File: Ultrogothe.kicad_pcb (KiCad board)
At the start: 2 copper layers, 20.3 x 54.6 mm, 18 parts, among them J1 Conn_01x20, J2 Conn_01x20, J3 Conn_02x05_Odd_Even, U1 XC6206PxxxMR, U2 STM32F103CBTx, Y1 Crystal

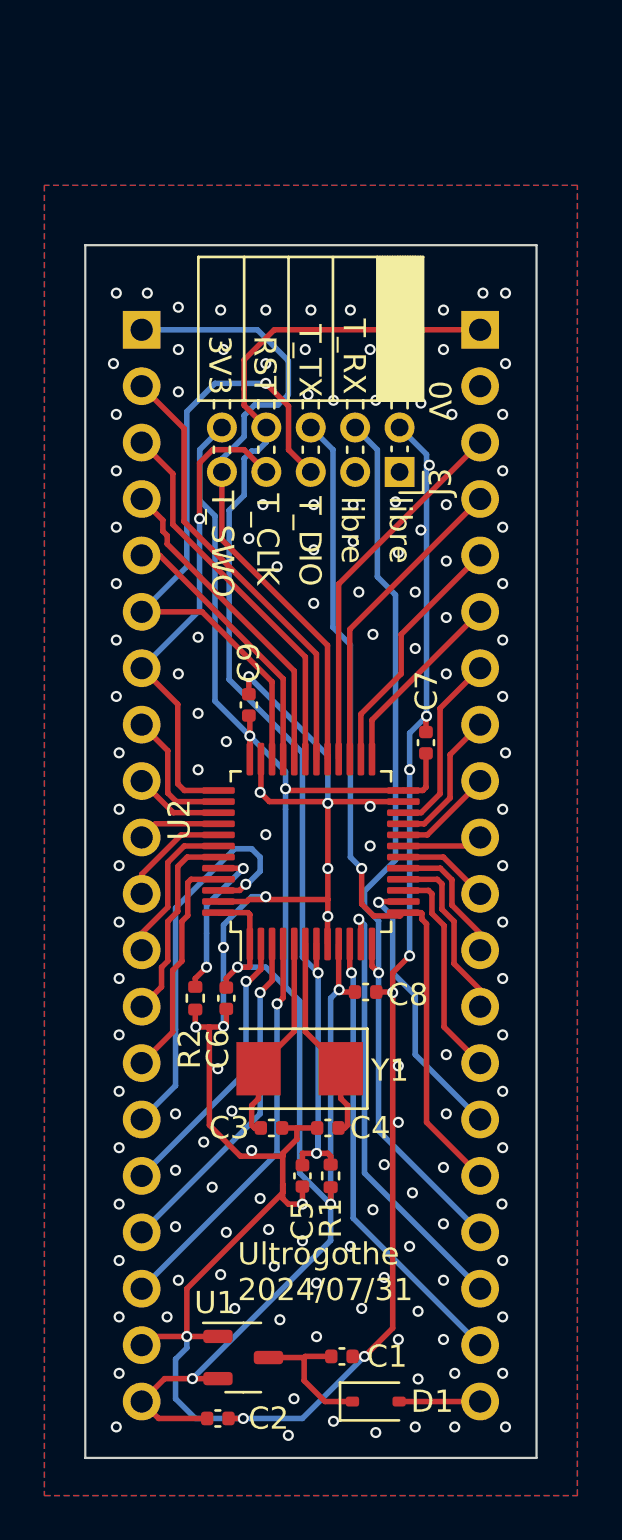
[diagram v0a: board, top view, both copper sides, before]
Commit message: Passage à kicad 8
et correction des chemins spécifiques
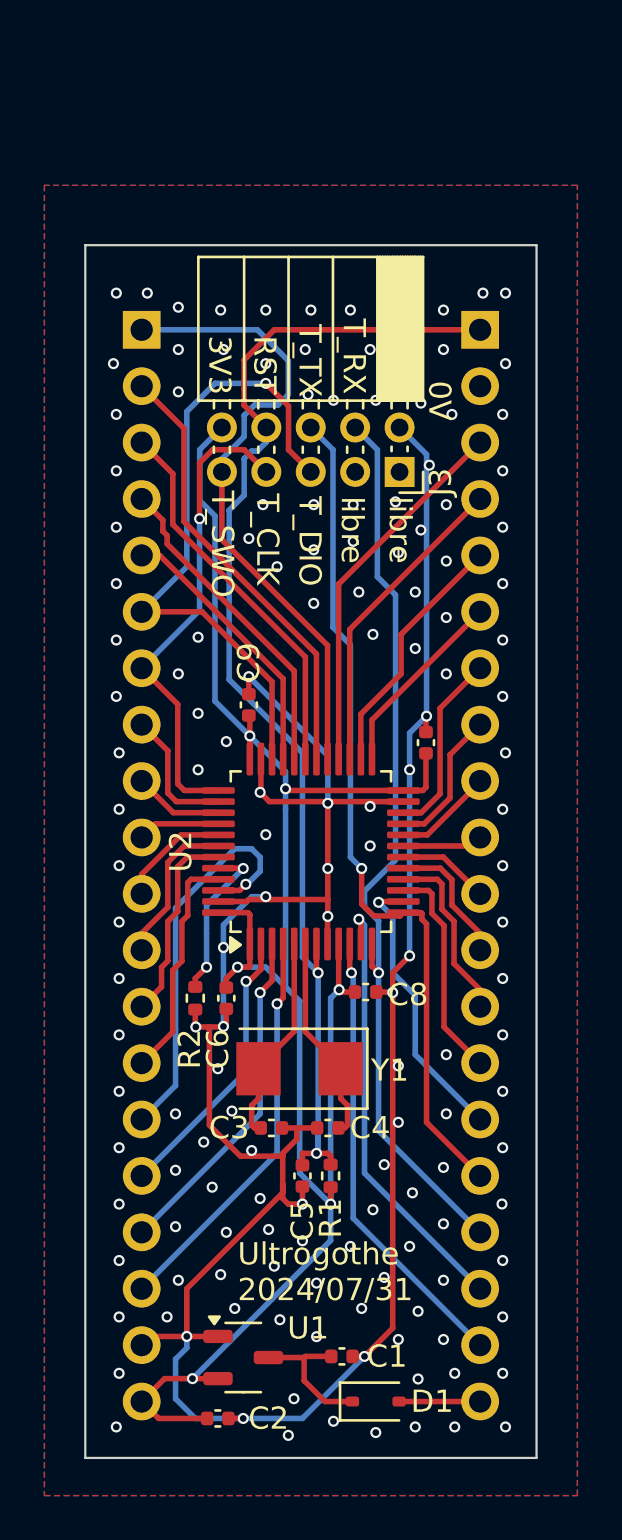
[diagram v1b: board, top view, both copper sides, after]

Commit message: Chgt connecteur programmation
passage à 2,54mm
alignement avec grille
silk: ajout pins
maj schéma pour clarification
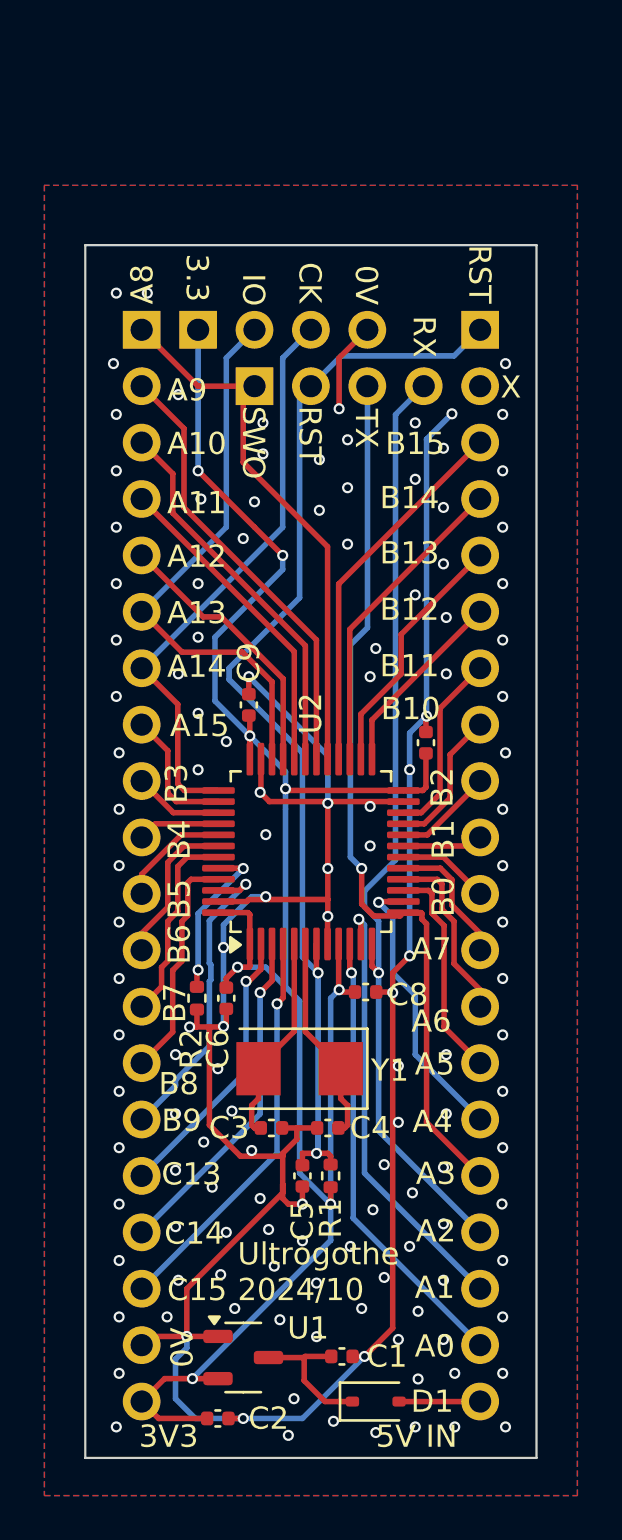
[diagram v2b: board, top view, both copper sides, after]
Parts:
- added J4: Conn_01x04, Chimere_comps:PinHeader_1x04_P2.54mm_Simple, B.Cu at (132.1, 53.3)
- J1, J2: footprint Connector_PinHeader_2.54mm:PinHeader_1x20_P2.54mm_Vertical -> Chimere_comps:PinHeader_1x20_P2.54mm_Simple
- J3: value Conn_02x05_Odd_Even -> Conn_01x04; footprint Connector_PinSocket_2.00mm:PinSocket_2x05_P2.00mm_Horizontal -> Chimere_comps:PinHeader_1x04_P2.54mm_Simple; moved to B.Cu
- moved J3 11.1 mm to (129.5, 50.8)
- moved R2 0.08 mm to (129.5, 80.9)
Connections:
- net /s_debugger/5V renamed /s_Alimentation/5V
- J3 pad 1: unconnected-(J3-Pin_1-Pad1) -> 3V3
- J3 pad 2: 0V -> A13
- J3 pad 3: unconnected-(J3-Pin_3-Pad3) -> A14
- J3 pad 4: A2 -> 0V
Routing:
- net 3V3: track 86.7 -> 93.2 mm, vias 6 -> 8
- net 0V: track 124.0 -> 128.9 mm, vias 153 -> 137
- net A14: track 21.8 -> 26.2 mm, vias 1 -> 0
- net B9: track 18.1 -> 13.9 mm
- net A13: track 29.4 -> 25.5 mm, vias 1 -> 0
- net A8: track 28.9 -> 25.4 mm
- net nRST: track 53.9 -> 50.4 mm
- net A2: track 41.2 -> 42.8 mm
- net A3: track 38.3 -> 39.8 mm
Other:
- board text added: "3.3"
- board text added: "5V IN"
- board text added: "A0"
- board text added: "A1"
- board text added: "A10"
- board text added: "A11"
- board text added: "A12"
- board text added: "A13"
- board text added: "A14"
- board text added: "A15"
- board text added: "A2"
- board text added: "A3"
- board text added: "A4"
- board text added: "A5"
- board text added: "A6"
- board text added: "A7"
- board text added: "A8"
- board text added: "A9"
- board text added: "B0"
- board text added: "B1"
- board text added: "B10"
- board text added: "B11"
- board text added: "B12"
- board text added: "B13"
- board text added: "B14"
- board text added: "B15"
- board text added: "B2"
- board text added: "B3"
- board text added: "B4"
- board text added: "B5"
- board text added: "B6"
- board text added: "B7"
- board text added: "B8"
- board text added: "B9"
- board text added: "C13"
- board text added: "C14"
- board text added: "C15"
- board text added: "CK"
- board text added: "IO"
- board text added: "RX"
- board text added: "SWO"
- board text added: "TX"
- board text added: "Ultrogothe 2024/10"
- board text added: "Ultrogothe 2024/10/23"
- board text added: "X"
- board text removed: "T_CLK"
- board text removed: "T_DIO"
- board text removed: "T_RX"
- board text removed: "T_SWO"
- board text removed: "T_TX"
- board text removed: "Ultrogothe 2024/07/31"
- board text removed: "libre"

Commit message: vias et plans cuivres
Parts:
- moved C2 0.13 mm to (130.4, 99.7)
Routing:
- net 3V3: track 93.2 -> 84.4 mm
- net 0V: track 128.9 -> 131.5 mm, vias 137 -> 196

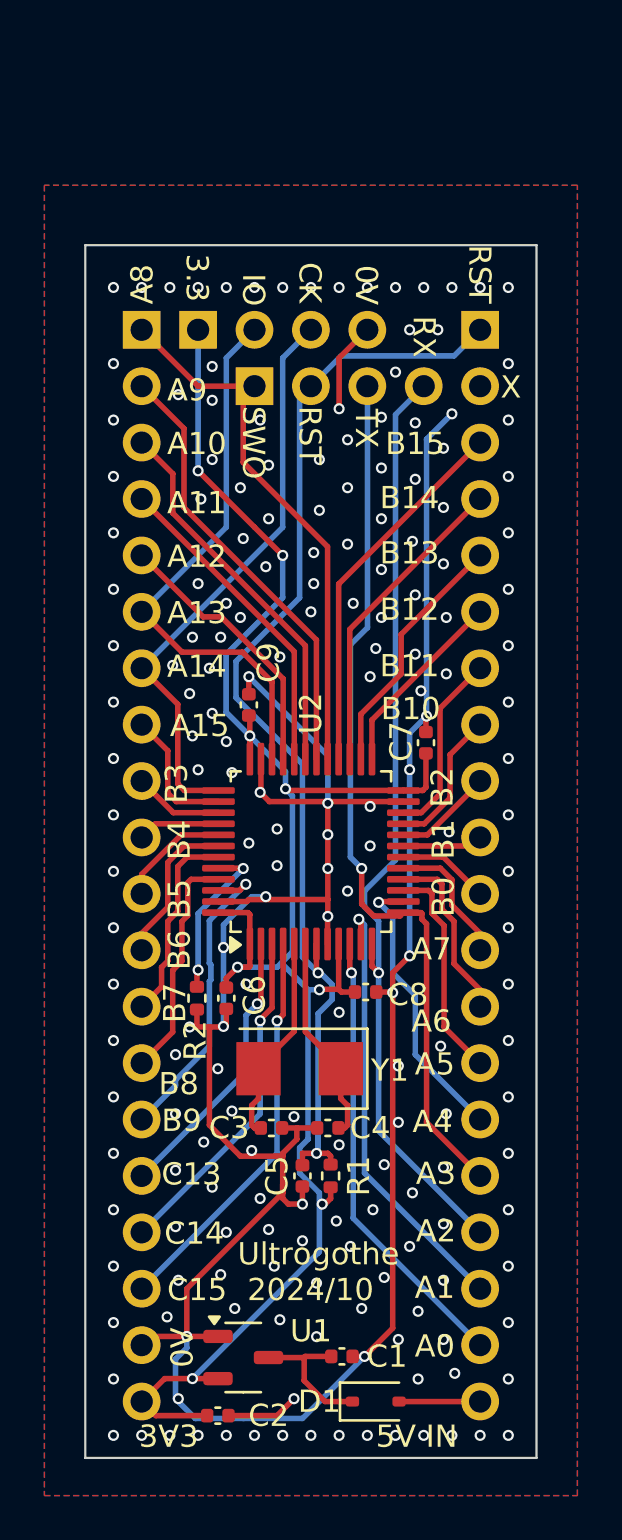
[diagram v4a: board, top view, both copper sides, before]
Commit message: changement connecteur prog/debug par ST14
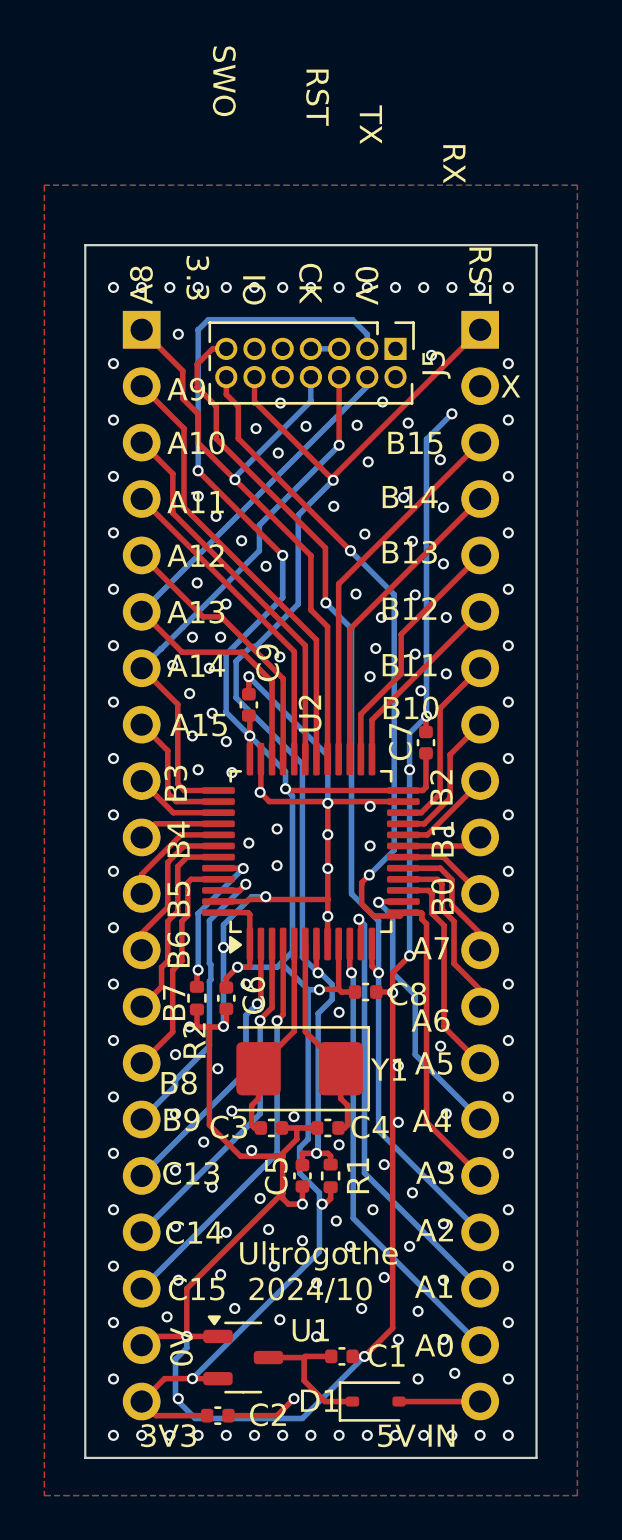
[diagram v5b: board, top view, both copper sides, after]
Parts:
- removed J3, J4: Conn_01x04, Chimere_comps:PinHeader_1x04_P2.54mm_Simple
- added J5: Conn_02x07_Odd_Even, Connector_PinHeader_1.27mm:PinHeader_2x07_P1.27mm_Vertical, F.Cu at (138.4, 51.7)
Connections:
- net 0V renamed /0V
- net 3V3 renamed /3V3
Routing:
- net /3V3: track 84.4 -> 93.1 mm
- net A2: track 42.8 -> 47.4 mm, vias 1 -> 2
- net A3: track 39.8 -> 43.4 mm, vias 1 -> 2
- net A8: track 25.4 -> 28.8 mm, vias 0 -> 1
- net nRST: track 50.8 -> 54.1 mm, vias 2 -> 3
- net /0V: track 131.5 -> 128.7 mm, vias 196 -> 182
- net A14: track 26.2 -> 24.6 mm, vias 0 -> 1

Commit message: chgt ST14 en CMS et fabrication
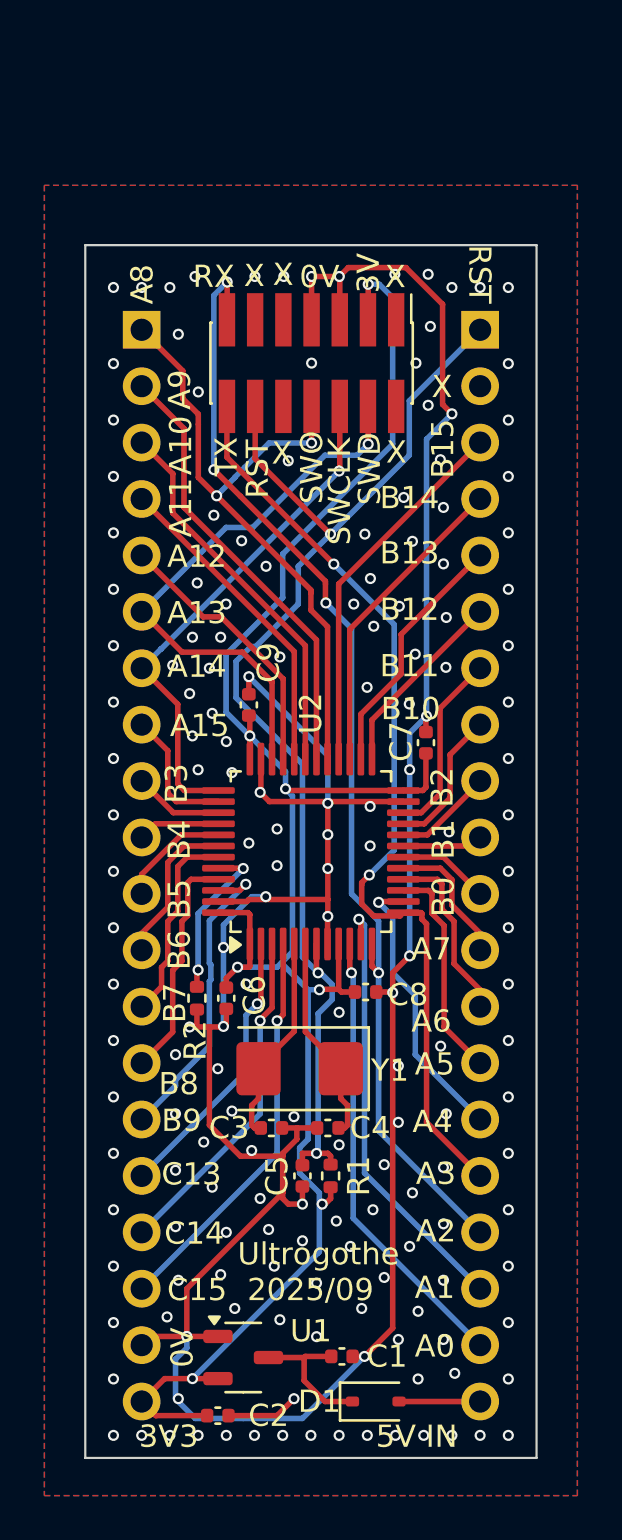
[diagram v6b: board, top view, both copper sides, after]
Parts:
- J5: footprint Connector_PinHeader_1.27mm:PinHeader_2x07_P1.27mm_Vertical -> Connector_PinHeader_1.27mm:PinHeader_2x07_P1.27mm_Vertical_SMD
- moved J5 3.83 mm to (134.7, 52.3)
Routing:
- net /0V: track 128.7 -> 143.2 mm, vias 182 -> 175
- net /3V3: track 93.1 -> 89.3 mm, vias 8 -> 7
- net A2: track 47.4 -> 51.1 mm, vias 2 -> 4
- net A3: track 43.4 -> 42.0 mm
- net A14: track 24.6 -> 23.3 mm
- net nRST: track 54.1 -> 55.1 mm
- net A8: track 28.8 -> 29.7 mm, vias 1 -> 2
- net A13: track 25.4 -> 25.7 mm, vias 0 -> 1
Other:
- board text added: "3V"
- board text added: "SWCLK"
- board text added: "SWD"
- board text added: "Ultrogothe 2025/09"
- board text added: "Ultrogothe 2025/09/21"
- board text removed: "3.3"
- board text removed: "CK"
- board text removed: "IO"
- board text removed: "Ultrogothe 2024/10"
- board text removed: "Ultrogothe 2024/10/23"
